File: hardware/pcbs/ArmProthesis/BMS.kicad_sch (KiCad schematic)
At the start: 54 parts, among them J1 XT60-M, J2 4-1971800-1, J3 XT60-M, Q1 NVMFS5C460NLWFAFT1G, Q2 NVMFS5C460NLWFAFT1G, Q3 BSS84, SW1 CK_KMS2xxG, SW2 CK_KMS2xxG, SW3 CK_KMS2xxG, U1 BQ76920PW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

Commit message: BMS v0.3 + main folder reconstruction
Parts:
- removed J2: 4-1971800-1, headers:XH_2.5mm, symbol headers:4-1971800-1
- removed J3: XT60-M, Custom_Connectors:XT60-M, symbol Custom_Connectors:XT60-M
- removed U5: ~, Connector_JST:JST_GH_BM05B-GHS-TBT_1x05-1MP_P1.25mm_Vertical, symbol headers:H_5
- removed U7: ~, Connector_PinHeader_2.54mm:PinHeader_1x11_P2.54mm_Vertical, symbol headers:H_11
- added H1, H2, H3, H4: MountingHole, MountingHole:MountingHole_3.2mm_M3_DIN965, symbol Mechanical:MountingHole
- added J2: XT60-F, Connector_AMASS:AMASS_XT60PW-F_1x02_P7.20mm_Horizontal, symbol Custom_Connectors:XT60-M
- added J3: 4-1971800-1, Connector_JST:JST_XH_S4B-XH-A_1x04_P2.50mm_Horizontal, symbol headers:4-1971800-1
- added U5: ~, Connector_PinHeader_2.54mm:PinHeader_2x05_P2.54mm_Horizontal, symbol headers:H_10
- C1, C2: footprint Capacitor_SMD:C_0805_2012Metric_Pad1.18x1.45mm_HandSolder -> Capacitor_SMD:C_0603_1608Metric_Pad1.08x0.95mm_HandSolder; Website http://eu.mouser.com/ProductDetail/Murata-Electronics/GCJ21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 -> https://eu.mouser.com/ProductDetail/TDK/C1608X7R1H105K080AB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
- C12, C15: footprint Capacitor_SMD:C_0603_1608Metric_Pad1.08x0.95mm_HandSolder -> Capacitor_SMD:C_0402_1005Metric_Pad0.74x0.62mm_HandSolder
- J1: footprint Custom_Connectors:XT60-M -> Connector_AMASS:AMASS_XT60PW-M_1x02_P7.20mm_Horizontal
- Q1, Q2: value NVMFS5C460NLWFAFT1G -> BSC014N04LSIATMA1; footprint MOSFET-N:MOSFET_N_NVMFS5C460NLWFAFT1G -> MOSFET-N:TRANS_BSC014N04LSIATMA1; Website https://eu.mouser.com/ProductDetail/onsemi/NVMFS5C460NLWFAF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 -> (none)
- U3, U4: footprint Connector_JST:JST_GH_BM02B-GHS-TBT_1x02-1MP_P1.25mm_Vertical -> Connector_JST:JST_GH_SM02B-GHS-TB_1x02-1MP_P1.25mm_Horizontal
- renumbered D8 to D2, R28 to R17, R26 to R18, R29 to R19
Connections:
- net GND: now also J1.1; no longer J1.N (NEG), Q1.3 (D), R9.1, U3.2, U4.2
- net PA0: now also U5.8
- net PA1: now also U5.7
- net PA11: now also U5.4
- net PA12: now also U5.3
- net PA13: now also U5.6
- net PA14: now also U5.5
- net PA2: now also U5.10
- net PA3: now also U5.9
- net PA5: now also U5.1
- net PA6: now also U5.2
- net PACK+: now also J1.2, U3.2, U4.2, J2.2; no longer J1.P (POS), U3.1, U4.1
- net at C8.1, C9.2, R4.2: now also J3.2
- net at C7.1, C8.2, R2.2: now also J3.3
- net at C9.1, R5.2: now also J3.1
- net at C6.2, R3.2: now also J3.4
- new net BMS_GND: J2.1, Q1.3 (D), R9.1, U3.1, U4.1
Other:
- moved on the sheet: D1

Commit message: .
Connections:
- net at R4.1, U1.13 (VC4), U1.14 (VC3)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: no longer R5.1, U1.12 (VC5)
- new net: R5.1, U1.12 (VC5)
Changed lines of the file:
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@@
-	)
-	(junction
-		(at 136.652 76.962)
-		(diameter 0)
-		(color 0 0 0 0)
 	)
 	(junction
@@
 	)
 	(junction
-		(at 136.652 74.422)
-		(diameter 0)
-		(color 0 0 0 0)
-	)
-	(junction
 		(at 69.088 29.464)
 		(diameter 0)
@@
 	(wire
 		(pts
-			(xy 136.652 74.422) (xy 135.636 74.422)
+			(xy 135.636 74.422) (xy 156.21 74.422)
 		)
 		(stroke
@@
 	(wire
 		(pts
-			(xy 156.21 74.422) (xy 136.652 74.422)
-		)
-		(stroke
-			(width 0)
-			(type default)
-		)
-	)
-	(wire
-		(pts
 			(xy 98.298 106.68) (xy 98.298 107.696)
 		)
@@
 		)
 		(stroke
-			(width 0)
-			(type default)
-		)
-	)
-	(wire
-		(pts
-			(xy 136.652 74.422) (xy 136.652 76.962)
-		)
-		(stroke

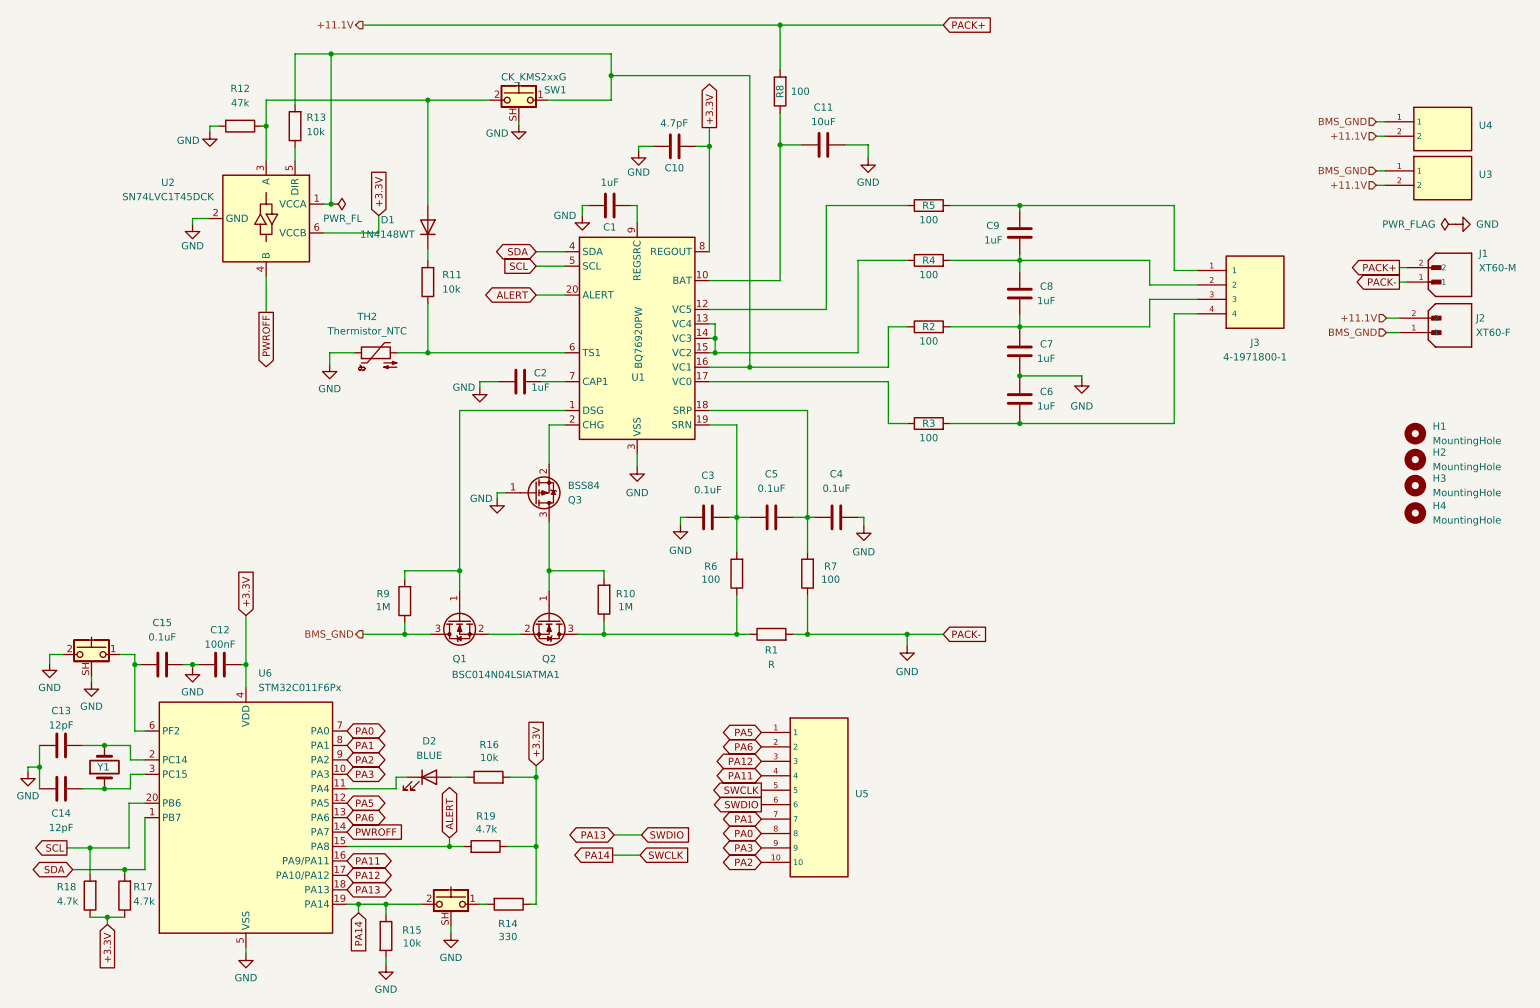
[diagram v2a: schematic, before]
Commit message: Corrected BMS connection
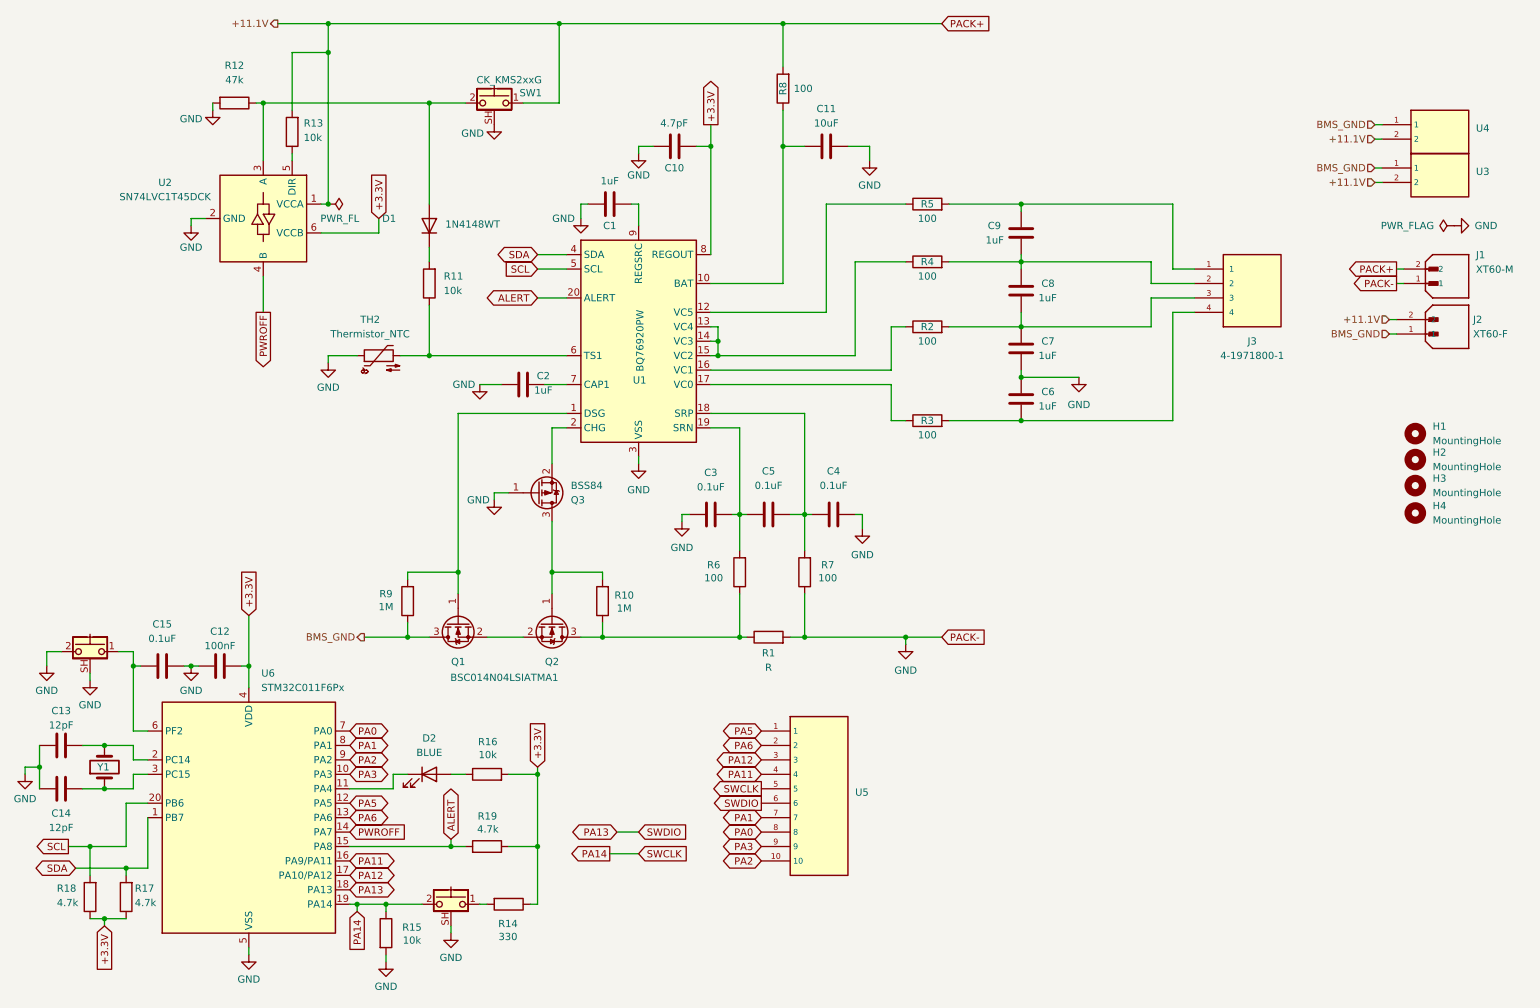
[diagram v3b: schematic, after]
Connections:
- net PACK+: now also R13.2, SW1.1, U2.1 (VCCA)
- new net: R2.1, U1.16 (VC1)
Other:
- moved on the sheet: C11, C2, C3, C4, C5, C7, C8, D2, J1, J2, J3, Q1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

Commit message: BMS v0.5 still not resized
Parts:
- removed R13: 10k, Resistor_SMD:R_0603_1608Metric_Pad0.98x0.95mm_HandSolder, symbol Device:R
- removed U2: SN74LVC1T45DCK, Package_TO_SOT_SMD:SOT-23-6_Handsoldering, symbol Logic_LevelTranslator:SN74LVC1T45DCK
- added SW4: CK_KMS2xxG, Button_Switch_SMD:SW_SPST_CK_KMS2xxG, symbol Switch:CK_KMS2xxG
- R12: value 47k -> 1k; footprint Resistor_SMD:R_0603_1608Metric_Pad0.98x0.95mm_HandSolder -> Resistor_SMD:R_0402_1005Metric_Pad0.72x0.64mm_HandSolder
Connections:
- net +3.3V: now also SW4.2
- net GND: now also SW4.SH (B); no longer R12.2
- net PA11: now also U5.3; no longer U5.4
- net PA12: now also U5.4; no longer U5.3
- net PACK+: no longer SW1.1
- net PWROFF: now also R12.1
- net at D1.2 (A), SW1.2: no longer R12.1
- net at R2.1, U1.16 (VC1): now also SW1.1
- new net: R12.2, SW4.1

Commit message: .
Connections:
- net PA13 renamed SWDIO
- net PA14 renamed SWCLK
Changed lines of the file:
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@@
-	(wire
-		(pts
-			(xy 119.38 166.37) (xy 123.19 166.37)
-		)
-		(stroke
-			(width 0)
-			(type default)
-		)
-	)
 	(wire
 		(pts
@@
 		(pts
 			(xy 105.41 156.21) (xy 105.41 168.91)
-		)
-		(stroke
-			(width 0)
-			(type default)
-		)
-	)
-	(wire
-		(pts
-			(xy 118.11 170.18) (xy 123.19 170.18)
 		)
 		(stroke
@@
 		)
 	)
-	(global_label "SWCLK"
+	(global_label "SWDIO"
 		(shape input)
-		(at 123.19 170.18 0)
-		(fields_autoplaced yes)
-		(effects
-			(font
-				(size 1.27 1.27)
-			)
-			(justify left)
-		)
-		(property "Intersheetrefs" "${INTERSHEET_REFS}"
-			(at 132.4042 170.18 0)
+		(at 72.39 176.53 0)
+		(fields_autoplaced yes)
+		(effects
+			(font
+				(size 1.27 1.27)
+			)
+			(justify left)
+		)
+		(property "Intersheetrefs" "${INTERSHEET_REFS}"
+			(at 81.2414 176.53 0)
 			(effects
 				(font
@@
 		)
 	)
-	(global_label "PA14"
-		(shape input)
-		(at 73.66 180.34 270)
-		(fields_autoplaced yes)
-		(effects
-			(font
-				(size 1.27 1.27)
-			)
-			(justify right)
-		)
-		(property "Intersheetrefs" "${INTERSHEET_REFS}"
-			(at 73.66 188.1028 90)
-			(effects
-				(font
-					(size 1.27 1.27)
-				)
-				(justify right)
-				(hide yes)
-			)
-		)
-	)
 	(global_label "PA2"
 		(shape bidirectional)
@@
 				)
 				(justify right)
-				(hide yes)
-			)
-		)
-	)
-	(global_label "PA13"
-		(shape bidirectional)
-		(at 72.39 176.53 0)
-		(fields_autoplaced yes)
-		(effects
-			(font
-				(size 1.27 1.27)
-			)
-			(justify left)
-		)
-		(property "Intersheetrefs" "${INTERSHEET_REFS}"
-			(at 80.1528 176.53 0)
-			(effects
-				(font
-					(size 1.27 1.27)
-				)
-				(justify left)
 				(hide yes)
 			)
@@
 		)
 	)
-	(global_label "PA14"
-		(shape output)
-		(at 118.11 170.18 180)
-		(fields_autoplaced yes)
-		(effects
-			(font
-				(size 1.27 1.27)
-			)
-			(justify right)
-		)
-		(property "Intersheetrefs" "${INTERSHEET_REFS}"
-			(at 110.3472 170.18 0)
-			(effects
-				(font
-					(size 1.27 1.27)
-				)
-				(justify right)
-				(hide yes)
-			)
-		)
-	)
 	(global_label "ALERT"
 		(shape bidirectional)
@@
 		)
 	)
-	(global_label "SWDIO"
+	(global_label "SWCLK"
 		(shape input)
-		(at 123.19 166.37 0)
-		(fields_autoplaced yes)
-		(effects
-			(font
-				(size 1.27 1.27)
-			)
-			(justify left)
-		)
-		(property "Intersheetrefs" "${INTERSHEET_REFS}"
-			(at 132.0414 166.37 0)
-			(effects
-				(font
-					(size 1.27 1.27)
-				)
-				(justify left)
-				(hide yes)
-			)
-		)
-	)
-	(global_label "PA13"
-		(shape bidirectional)
-		(at 119.38 166.37 180)
-		(fields_autoplaced yes)
-		(effects
-			(font
-				(size 1.27 1.27)
-			)
-			(justify right)
-		)
-		(property "Intersheetrefs" "${INTERSHEET_REFS}"
-			(at 110.5059 166.37 0)
-			(effects
-				(font
+		(at 73.66 180.34 270)
+		(fields_autoplaced yes)
+		(effects
+			(font
+				(size 1.27 1.27)
+			)
+			(justify right)
+		)
+		(property "Intersheetrefs" "${INTERSHEET_REFS}"
+			(at 73.66 189.5542 90)
+			(effects
+				(font

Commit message: updates
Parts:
- removed C15: 0.1uF, Capacitor_SMD:C_0402_1005Metric_Pad0.74x0.62mm_HandSolder, symbol Device:C
- removed R14: 330, Resistor_SMD:R_0402_1005Metric_Pad0.72x0.64mm_HandSolder, symbol Device:R
- removed R15: 10k, Resistor_SMD:R_0402_1005Metric_Pad0.72x0.64mm_HandSolder, symbol Device:R
- removed SW3: CK_KMS2xxG, Button_Switch_SMD:SW_SPST_CK_KMS2xxG, symbol Switch:CK_KMS2xxG
- C1, C2: footprint Capacitor_SMD:C_0603_1608Metric_Pad1.08x0.95mm_HandSolder -> Capacitor_SMD:C_0603_1608Metric; LCSC (none) -> C15849; Website https://eu.mouser.com/ProductDetail/TDK/C1608X7R1H105K080AB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 -> (none)
- C10: footprint Capacitor_SMD:C_0402_1005Metric_Pad0.74x0.62mm_HandSolder -> Capacitor_SMD:C_0402_1005Metric; LCSC (none) -> C167420
- C11: footprint Capacitor_SMD:C_1210_3225Metric_Pad1.33x2.70mm_HandSolder -> Capacitor_SMD:C_1210_3225Metric; LCSC (none) -> C2918502
- C12: footprint Capacitor_SMD:C_0402_1005Metric_Pad0.74x0.62mm_HandSolder -> Capacitor_SMD:C_0402_1005Metric; LCSC (none) -> C110251
- C13, C14: footprint Capacitor_SMD:C_0603_1608Metric_Pad1.08x0.95mm_HandSolder -> Capacitor_SMD:C_0603_1608Metric; LCSC (none) -> C346206
- C3, C4, C5: footprint Capacitor_SMD:C_0603_1608Metric_Pad1.08x0.95mm_HandSolder -> Capacitor_SMD:C_0603_1608Metric; LCSC (none) -> C14663
- C6, C7, C8, C9: footprint Capacitor_SMD:C_0805_2012Metric_Pad1.18x1.45mm_HandSolder -> Capacitor_SMD:C_0603_1608Metric; LCSC (none) -> C15849; Website http://eu.mouser.com/ProductDetail/Murata-Electronics/GCJ21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 -> (none)
- D1: LCSC (none) -> C232841
- D2: footprint Diode_SMD:D_0603_1608Metric_Pad1.05x0.95mm_HandSolder -> Diode_SMD:D_0603_1608Metric; LCSC (none) -> C282129
- J3: LCSC (none) -> C157925
- Q1, Q2: LCSC (none) -> C2934854
- Q3: LCSC (none) -> C85202
- R1: value R -> 5m; footprint Resistor:R_3920 -> Resistor_SMD:R_2512_6332Metric; LCSC (none) -> C22385263
- R10, R9: footprint Resistor_SMD:R_0603_1608Metric_Pad0.98x0.95mm_HandSolder -> Resistor_SMD:R_0603_1608Metric; LCSC (none) -> C22935
- R11: footprint Resistor_SMD:R_0603_1608Metric_Pad0.98x0.95mm_HandSolder -> Resistor_SMD:R_0402_1005Metric; LCSC (none) -> C60490
- R12: footprint Resistor_SMD:R_0402_1005Metric_Pad0.72x0.64mm_HandSolder -> Resistor_SMD:R_0402_1005Metric; LCSC (none) -> C11702
- R16: footprint Resistor_SMD:R_0402_1005Metric_Pad0.72x0.64mm_HandSolder -> Resistor_SMD:R_0402_1005Metric; LCSC (none) -> C60490
- R17, R18, R19: footprint Resistor_SMD:R_0603_1608Metric_Pad0.98x0.95mm_HandSolder -> Resistor_SMD:R_0402_1005Metric; LCSC (none) -> C25900
- R2, R3, R4, R5, R6, R7, R8: footprint Resistor_SMD:R_0402_1005Metric_Pad0.72x0.64mm_HandSolder -> Resistor_SMD:R_0402_1005Metric; LCSC (none) -> C106232
- TH2: LCSC (none) -> C13564
- U1: LCSC (none) -> C181647
- U3, U4: LCSC (none) -> C189893
- U6: LCSC (none) -> C5456198
- Y1: LCSC (none) -> C519280
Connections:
- net GND: now also R12.2
- net PWROFF: now also SW4.1
- net at C1.2, U1.9 (REGSRC): now also R5.1, U1.12 (VC5)
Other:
- moved on the sheet: R12
